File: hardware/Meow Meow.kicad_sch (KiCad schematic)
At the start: 30 parts, among them J1 Conn_Left, J2 Conn_Right, J3 Conn_01x06, P1 SPACE, P10 A, P11 W, P12 KEY_UP_ARROW, P2 KEY_DOWN_ARROW, P3 KEY_RIGHT_ARROW, P5 KEY_LEFT_ARROW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

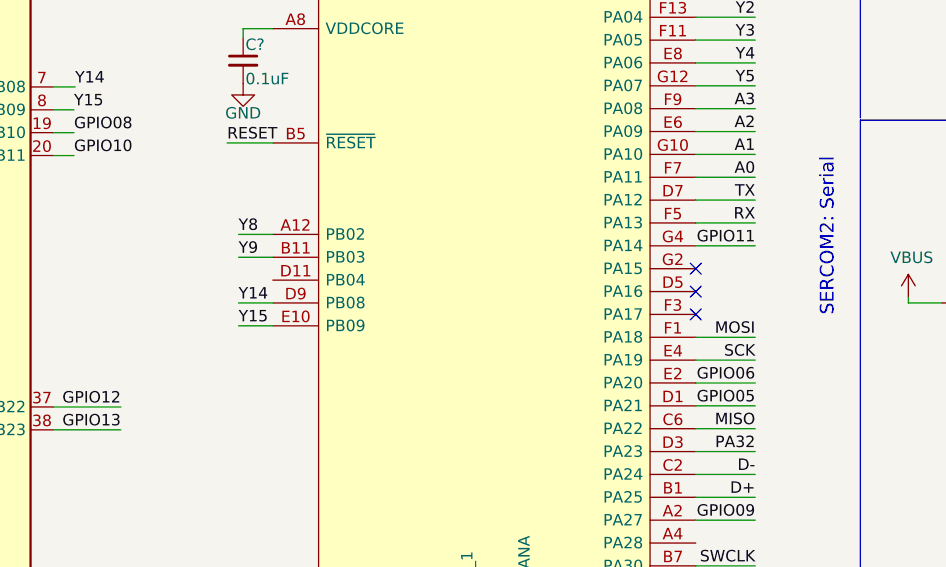
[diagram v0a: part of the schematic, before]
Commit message: new GPIOs
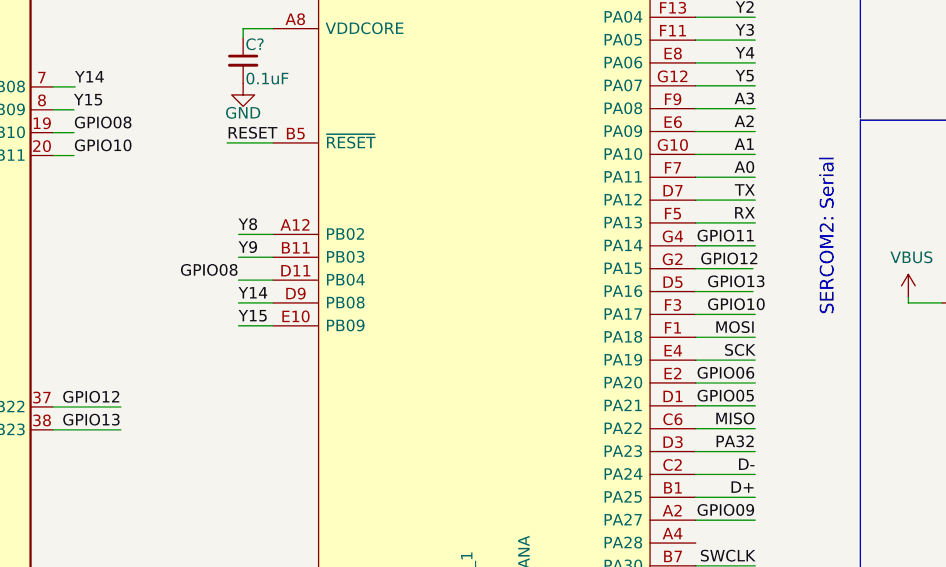
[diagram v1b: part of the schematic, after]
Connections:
- net GPIO08: now also U?.D11 (PB04)
- net GPIO10: now also U?.F3 (PA17)
- net GPIO12: now also U?.G2 (PA15)
- net GPIO13: now also U?.D5 (PA16)
- no-connect marks 15 -> 12
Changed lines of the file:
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@@
   (no_connect (at 76.835 172.593))
   (no_connect (at 193.929 87.884))
-  (no_connect (at 158.75 76.454))
-  (no_connect (at 158.75 78.994))
-  (no_connect (at 158.75 81.534))
   (no_connect (at 48.387 107.061))
   (no_connect (at 228.092 96.012))
@@
     (stroke (width 0) (type default) (color 0 0 0 0))
   )
+  (wire (pts (xy 107.95 77.724) (xy 111.76 77.724))
+    (stroke (width 0) (type default) (color 0 0 0 0))
+  )
   (wire (pts (xy 106.045 172.593) (xy 107.315 172.593))
     (stroke (width 0) (type default) (color 0 0 0 0))
@@
     (stroke (width 0) (type default) (color 0 0 0 0))
   )
+  (wire (pts (xy 158.75 81.534) (xy 165.354 81.534))
+    (stroke (width 0) (type default) (color 0 0 0 0))
+  )
   (wire (pts (xy 109.22 38.354) (xy 109.22 33.02))
     (stroke (width 0) (type default) (color 0 0 0 0))
@@
     (stroke (width 0) (type default) (color 0 0 0 0))
   )
+  (wire (pts (xy 158.75 78.994) (xy 165.1 78.994))
+    (stroke (width 0) (type default) (color 0 0 0 0))
+  )
   (wire (pts (xy 69.596 126.746) (xy 70.866 126.746))
     (stroke (width 0) (type default) (color 0 0 0 0))
@@
   )
   (wire (pts (xy 191.262 90.424) (xy 191.262 91.44))
+    (stroke (width 0) (type default) (color 0 0 0 0))
+  )
+  (wire (pts (xy 158.75 76.454) (xy 165.1 76.454))
     (stroke (width 0) (type default) (color 0 0 0 0))
   )
@@
     (effects (font (size 1.27 1.27)) (justify left bottom))
   )
+  (label "GPIO13" (at 160.02 78.994 0)
+    (effects (font (size 1.27 1.27)) (justify left bottom))
+  )
   (label "Y2" (at 165.354 48.514 180)
     (effects (font (size 1.27 1.27)) (justify right bottom))
@@
     (effects (font (size 1.27 1.27)) (justify right bottom))
   )
+  (label "GPIO08" (at 107.95 77.724 180)
+    (effects (font (size 1.27 1.27)) (justify right bottom))
+  )
   (label "Y14" (at 89.789 56.261 0)
     (effects (font (size 1.27 1.27)) (justify left bottom))
@@
     (effects (font (size 1.27 1.27)) (justify right bottom))
   )
+  (label "GPIO12" (at 159.258 76.454 0)
+    (effects (font (size 1.27 1.27)) (justify left bottom))
+  )
   (label "GPIO06" (at 165.354 89.154 180)
     (effects (font (size 1.27 1.27)) (justify right bottom))
@@
     (effects (font (size 1.27 1.27)) (justify left bottom))
   )
+  (label "GPIO10" (at 160.02 81.534 0)
+    (effects (font (size 1.27 1.27)) (justify left bottom))
+  )
